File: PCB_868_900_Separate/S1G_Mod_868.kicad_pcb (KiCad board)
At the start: 4 copper layers, 60 x 33.3 mm, 91 parts, among them J2 20021121-00010C4LF, J5 0475890001-MicroUSBPort, P1 61301621121, Q1 DMG2307L-7, SW1 CUS-12TB, SW2 B3U-1000P, T1 0732511150, T2 0732511150, U1 AP7361-33FGE-7, U2 ADF7023BCPZ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

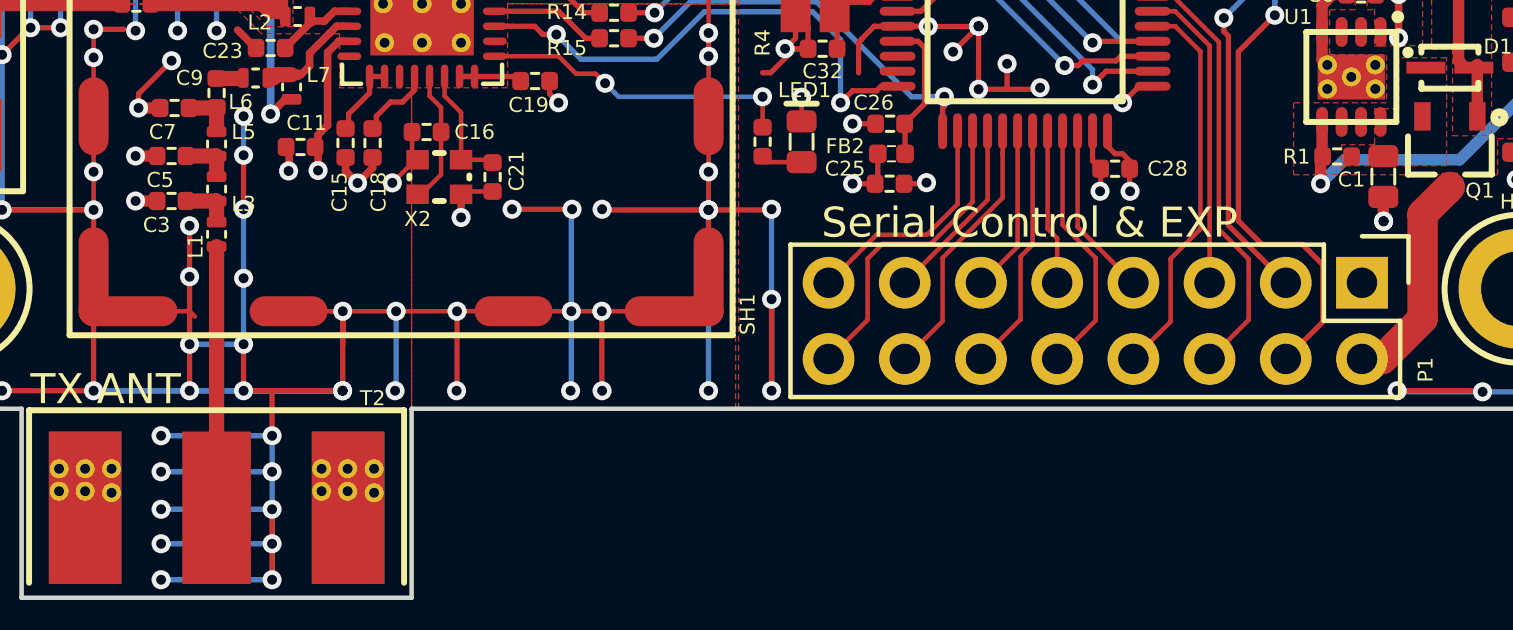
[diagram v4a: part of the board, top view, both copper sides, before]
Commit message: More Stitching and readme
Added more via stitching to separate RX/TX implementation. More vias
near the pin connector like the combined version. Also added a link to
the firmware repo on the readme.
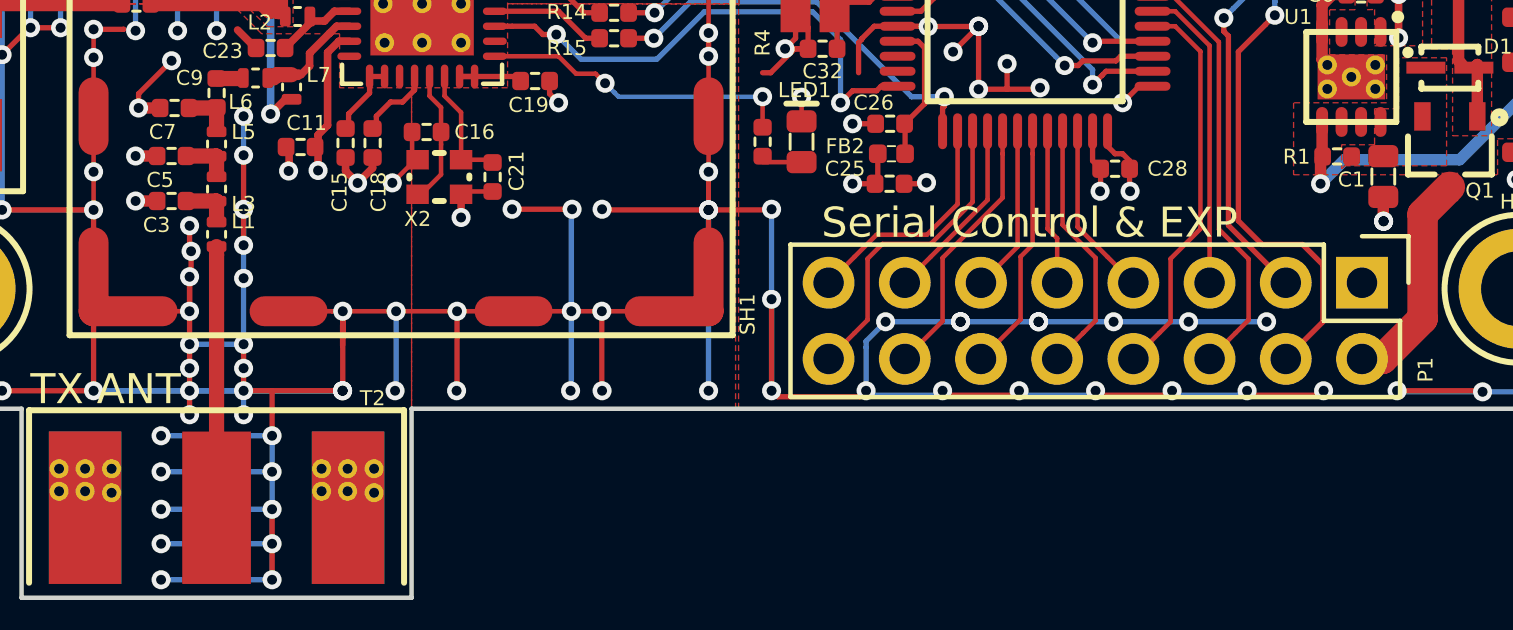
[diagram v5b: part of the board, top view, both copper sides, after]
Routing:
- net GND: track 435.3 -> 473.9 mm, vias 176 -> 198
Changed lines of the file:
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@@
     (thickness 1.6)
     (drawings 22)
-    (tracks 1004)
+    (tracks 1066)
     (zones 0)
     (modules 91)
@@
     (38 B.Mask user)
     (39 F.Mask user)
-    (40 Dwgs.User user hide)
+    (40 Dwgs.User user)
     (41 Cmts.User user)
     (42 Eco1.User user)
@@
   (module PCB_Footprints:L0402 (layer F.Cu)
     (at 69.2 56.185 90)
-    (fp_text reference L1 (at -0.4 -0.7 90) (layer F.SilkS)
+    (fp_text reference L1 (at 0.435 0.9 180) (layer F.SilkS)
       (effects (font (size 0.5 0.5) (thickness 0.1)))
     )
@@
   (gr_line (start 62.7 68.3) (end 75.7 68.3) (layer Edge.Cuts) (width 0.15))
   (gr_line (start 56.5 35) (end 56.5 62) (layer Edge.Cuts) (width 0.15))
+  (segment (start 101.6 59.1) (end 104.2 59.1) (width 0.1778) (layer B.Cu) (net 1))
+  (via (at 104.2 59.1) (size 0.635) (drill 0.3302) (layers F.Cu B.Cu) (net 1))
+  (segment (start 99.1 59.1) (end 101.6 59.1) (width 0.1778) (layer B.Cu) (net 1))
+  (via (at 101.6 59.1) (size 0.635) (drill 0.3302) (layers F.Cu B.Cu) (net 1))
+  (segment (start 96.6 59.1) (end 99.1 59.1) (width 0.1778) (layer B.Cu) (net 1))
+  (via (at 99.1 59.1) (size 0.635) (drill 0.3302) (layers F.Cu B.Cu) (net 1))
+  (via (at 96.6 59.1) (size 0.635) (drill 0.3302) (layers F.Cu B.Cu) (net 1))
+  (segment (start 94 59.1) (end 96.6 59.1) (width 0.1778) (layer B.Cu) (net 1))
+  (via (at 96.6 59.1) (size 0.635) (drill 0.3302) (layers F.Cu B.Cu) (net 1))
+  (via (at 94 59.1) (size 0.635) (drill 0.3302) (layers F.Cu B.Cu) (net 1))
+  (segment (start 91.5 59.1) (end 94 59.1) (width 0.1778) (layer B.Cu) (net 1))
+  (via (at 94 59.1) (size 0.635) (drill 0.3302) (layers F.Cu B.Cu) (net 1))
+  (segment (start 90.85 59.954746) (end 90.85 59.75) (width 0.1778) (layer B.Cu) (net 1))
+  (segment (start 90.85 59.75) (end 91.5 59.1) (width 0.1778) (layer B.Cu) (net 1))
+  (via (at 91.5 59.1) (size 0.635) (drill 0.3302) (layers F.Cu B.Cu) (net 1))
+  (segment (start 90.85 61.4) (end 90.85 59.954746) (width 0.1778) (layer B.Cu) (net 1))
+  (segment (start 103.55 61.4) (end 103.7 61.55) (width 0.1778) (layer F.Cu) (net 1))
+  (segment (start 103.7 61.55) (end 105.95 61.55) (width 0.1778) (layer F.Cu) (net 1))
+  (segment (start 105.95 61.55) (end 106.1 61.4) (width 0.1778) (layer F.Cu) (net 1))
+  (segment (start 101.05 61.4) (end 101.2 61.55) (width 0.1778) (layer B.Cu) (net 1))
+  (segment (start 101.2 61.55) (end 103.4 61.55) (width 0.1778) (layer B.Cu) (net 1))
+  (segment (start 103.4 61.55) (end 103.55 61.4) (width 0.1778) (layer B.Cu) (net 1))
+  (segment (start 98.5 61.4) (end 98.65 61.55) (width 0.1778) (layer F.Cu) (net 1))
+  (segment (start 98.65 61.55) (end 100.9 61.55) (width 0.1778) (layer F.Cu) (net 1))
+  (segment (start 100.9 61.55) (end 101.05 61.4) (width 0.1778) (layer F.Cu) (net 1))
+  (segment (start 95.95 61.4) (end 96.1 61.55) (width 0.1778) (layer B.Cu) (net 1))
+  (segment (start 96.1 61.55) (end 98.35 61.55) (width 0.1778) (layer B.Cu) (net 1))
+  (segment (start 98.35 61.55) (end 98.5 61.4) (width 0.1778) (layer B.Cu) (net 1))
+  (segment (start 93.4 61.4) (end 93.55 61.55) (width 0.1778) (layer F.Cu) (net 1))
+  (segment (start 93.55 61.55) (end 95.8 61.55) (width 0.1778) (layer F.Cu) (net 1))
+  (segment (start 95.8 61.55) (end 95.95 61.4) (width 0.1778) (layer F.Cu) (net 1))
+  (segment (start 90.85 61.4) (end 91 61.55) (width 0.1778) (layer B.Cu) (net 1))
+  (segment (start 91 61.55) (end 93.25 61.55) (width 0.1778) (layer B.Cu) (net 1))
+  (segment (start 93.25 61.55) (end 93.4 61.4) (width 0.1778) (layer B.Cu) (net 1))
+  (via (at 106.1 61.4) (size 0.635) (drill 0.3302) (layers F.Cu B.Cu) (net 1))
+  (via (at 103.55 61.4) (size 0.635) (drill 0.3302) (layers F.Cu B.Cu) (net 1))
+  (via (at 101.05 61.4) (size 0.635) (drill 0.3302) (layers F.Cu B.Cu) (net 1))
+  (via (at 98.5 61.4) (size 0.635) (drill 0.3302) (layers F.Cu B.Cu) (net 1))
+  (via (at 95.95 61.4) (size 0.635) (drill 0.3302) (layers F.Cu B.Cu) (net 1))
+  (via (at 93.4 61.4) (size 0.635) (drill 0.3302) (layers F.Cu B.Cu) (net 1))
+  (segment (start 87.7 61.4) (end 87.9 61.6) (width 0.1778) (layer F.Cu) (net 1))
+  (segment (start 87.9 61.6) (end 90.65 61.6) (width 0.1778) (layer F.Cu) (net 1))
+  (segment (start 90.65 61.6) (end 90.85 61.4) (width 0.1778) (layer F.Cu) (net 1))
+  (via (at 90.85 61.4) (size 0.635) (drill 0.3302) (layers F.Cu B.Cu) (net 1))
+  (segment (start 70.1 61.4) (end 70.1 62.2) (width 0.1778) (layer B.Cu) (net 1))
+  (via (at 70.1 62.2) (size 0.635) (drill 0.3302) (layers F.Cu B.Cu) (net 1))
+  (segment (start 68.3 61.4) (end 68.3 62.2) (width 0.1778) (layer F.Cu) (net 1))
+  (via (at 68.3 62.2) (size 0.635) (drill 0.3302) (layers F.Cu B.Cu) (net 1))
+  (segment (start 68.3 60.65) (end 68.3 61.4) (width 0.1778) (layer F.Cu) (net 1))
+  (segment (start 68.3 59.85) (end 68.3 60.65) (width 0.1778) (layer F.Cu) (net 1))
+  (via (at 68.3 60.65) (size 0.635) (drill 0.3302) (layers F.Cu B.Cu) (net 1))
+  (segment (start 70.1 61.4) (end 70.1 60.65) (width 0.1778) (layer F.Cu) (net 1))
+  (segment (start 70.1 59.85) (end 70.1 60.65) (width 0.1778) (layer F.Cu) (net 1))
+  (via (at 70.1 60.65) (size 0.635) (drill 0.3302) (layers F.Cu B.Cu) (net 1))
+  (segment (start 68.3 57.6) (end 68.3 58.7481) (width 0.1778) (layer F.Cu) (net 1))
+  (segment (start 68.3 58.7481) (end 68.2981 58.75) (width 0.1778) (layer F.Cu) (net 1))
+  (via (at 68.2981 58.75) (size 0.635) (drill 0.3302) (layers F.Cu B.Cu) (net 1))
+  (segment (start 68.35 57.55) (end 68.35 56.75) (width 0.1778) (layer F.Cu) (net 1))
+  (segment (start 68.3 55.9) (end 68.3 56.7) (width 0.1778) (layer F.Cu) (net 1))
+  (segment (start 68.3 56.7) (end 68.35 56.75) (width 0.1778) (layer F.Cu) (net 1))
+  (via (at 68.35 56.75) (size 0.635) (drill 0.3302) (layers F.Cu B.Cu) (net 1))
+  (segment (start 70.1 57.65) (end 70.1 56.55) (width 0.1778) (layer B.Cu) (net 1))
+  (segment (start 70.1 56.55) (end 70.1 55.35) (width 0.1778) (layer B.Cu) (net 1))
+  (segment (start 70.1 55.35) (end 70.1 56.55) (width 0.1778) (layer F.Cu) (net 1))
+  (via (at 70.1 56.55) (size 0.635) (drill 0.3302) (layers F.Cu B.Cu) (net 1))
+  (segment (start 68.3 57.6) (end 68.35 57.55) (width 0.1778) (layer F.Cu) (net 1))
   (segment (start 101 44.017) (end 100.267 44.017) (width 0.1778) (layer F.Cu) (net 1))
   (segment (start 100.267 44.017) (end 100.25 44) (width 0.1778) (layer F.Cu) (net 1))
@@
   (segment (start 115.57 59.079891) (end 115.91865 59.428541) (width 0.1778) (layer B.Cu) (net 1))
   (via (at 115.91865 59.428541) (size 0.635) (drill 0.3302) (layers F.Cu B.Cu) (net 1))
-  (segment (start 68.3 57.6) (end 68.3 55.9) (width 0.1778) (layer F.Cu) (net 1))
   (via (at 68.3 55.9) (size 0.635) (drill 0.3302) (layers F.Cu B.Cu) (net 1))
   (segment (start 63 49.3) (end 64 49.3) (width 0.1778) (layer F.Cu) (net 1))
@@
   (segment (start 70.1 55.35) (end 70.1 53.55) (width 0.1778) (layer F.Cu) (net 1))
   (via (at 70.1 53.55) (size 0.635) (drill 0.3302) (layers F.Cu B.Cu) (net 1))
-  (segment (start 70.1 57.65) (end 70.1 55.35) (width 0.1778) (layer B.Cu) (net 1))
   (via (at 70.1 55.35) (size 0.635) (drill 0.3302) (layers F.Cu B.Cu) (net 1))
   (segment (start 70.1 59.85) (end 70.1 57.65) (width 0.1778) (layer B.Cu) (net 1))
@@
   (segment (start 73.4 61.4) (end 68.3 61.4) (width 0.1778) (layer B.Cu) (net 1))
   (segment (start 68.3 61.4) (end 65.75 61.4) (width 0.1778) (layer B.Cu) (net 1))
-  (segment (start 68.3 59.85) (end 68.3 61.4) (width 0.1778) (layer F.Cu) (net 1))
   (via (at 68.3 61.4) (size 0.635) (drill 0.3302) (layers F.Cu B.Cu) (net 1))
   (segment (start 70.1 59.85) (end 68.3 59.85) (width 0.1778) (layer B.Cu) (net 1))
   (via (at 68.3 59.85) (size 0.635) (drill 0.3302) (layers F.Cu B.Cu) (net 1))
-  (segment (start 70.1 61.4) (end 70.1 59.85) (width 0.1778) (layer F.Cu) (net 1))
   (via (at 70.1 59.85) (size 0.635) (drill 0.3302) (layers F.Cu B.Cu) (net 1))
   (segment (start 73.4 61.4) (end 70.1 61.4) (width 0.1778) (layer B.Cu) (net 1))
